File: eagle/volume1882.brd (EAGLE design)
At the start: 48.3 x 48.3 mm, 39 parts, among them IC1 LM317, IC2 LM337, U1 DS1882, U2 ATMEGA328P_TQFP

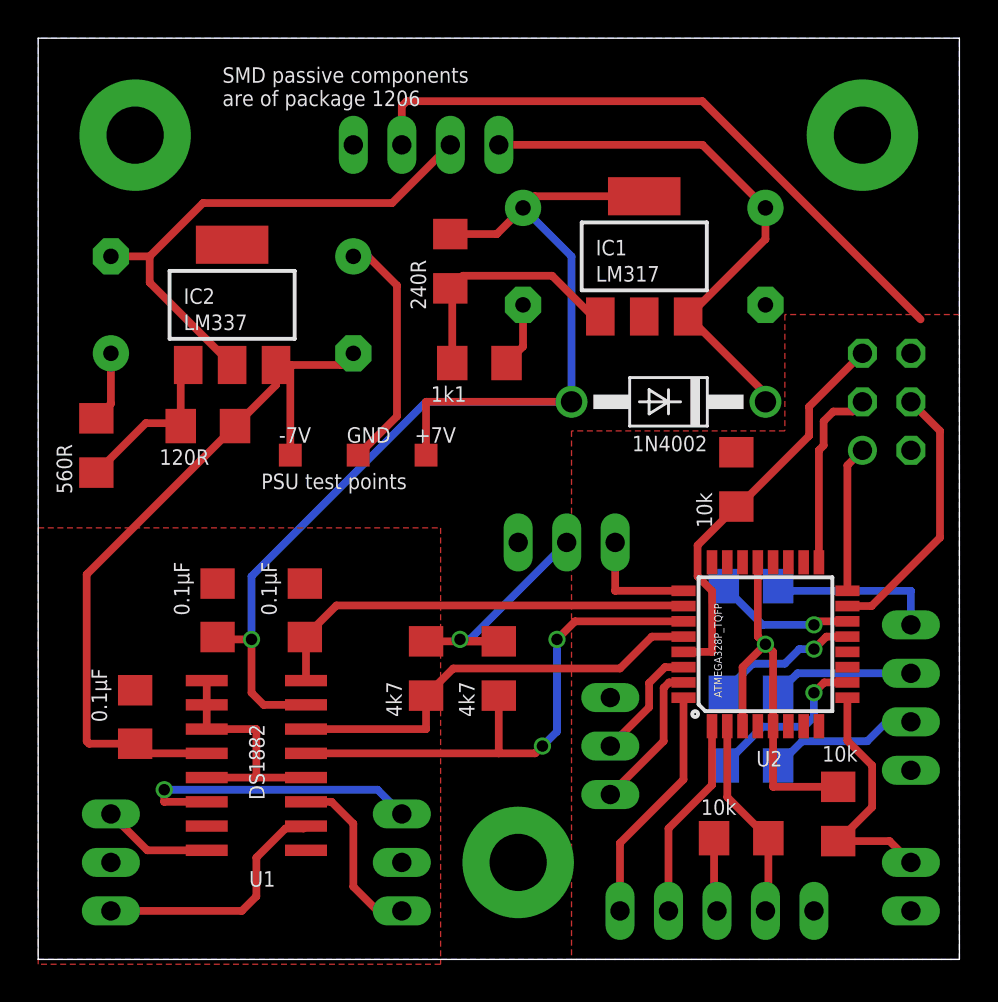
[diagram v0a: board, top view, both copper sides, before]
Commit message: fixed wrong size parts
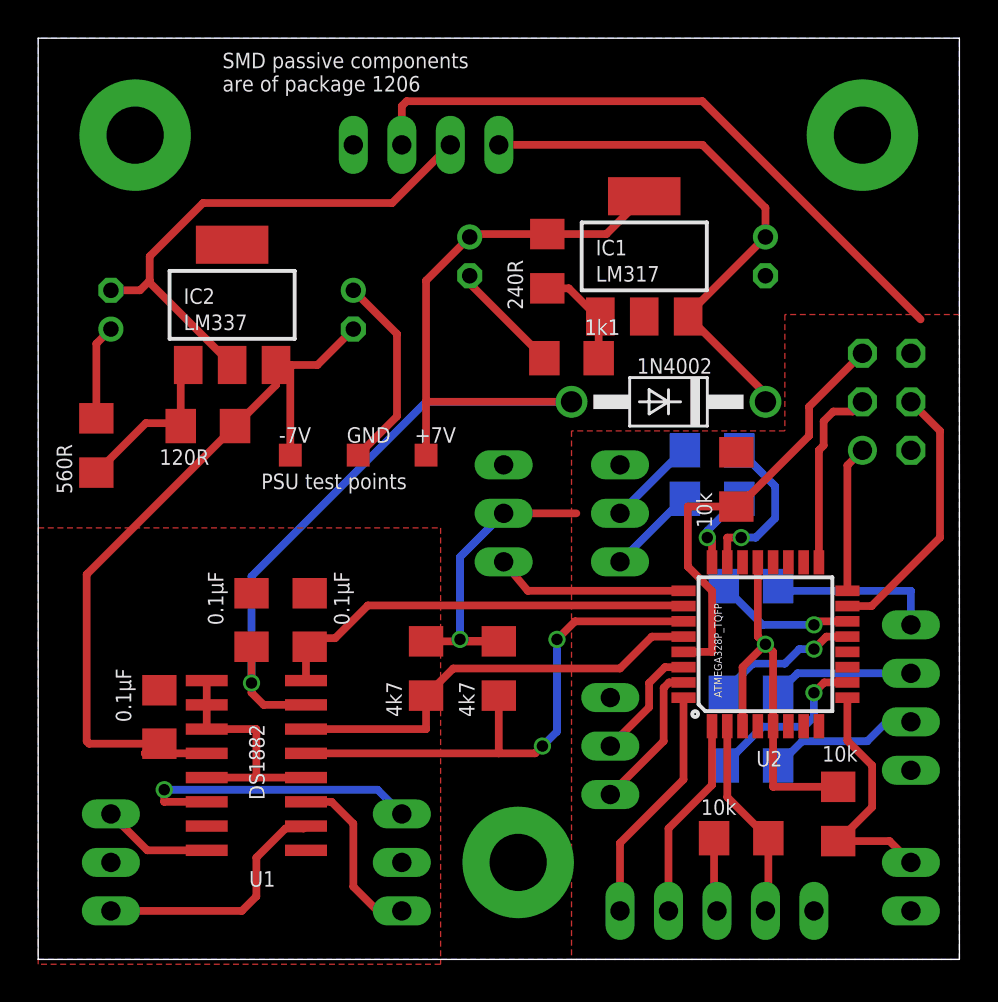
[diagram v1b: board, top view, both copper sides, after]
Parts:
- removed C4: 0.1µF, resistor:E5-5
- removed C5, C6: 1µF, resistor:E5-5
- removed C7: 10µF, resistor:E5-5
- added C10, C8: 1µF, resistor:E2-5
- added C11: 0.1µF, resistor:E2-5
- added C9: 10µF, resistor:E2-5
- added LED_OUTPUT: (no value), con-lstb:MA03-1
- added R13, R14: 470R, resistor:R1206
- moved R4 5.08 mm to (26.7, 36.6)
- moved R6 4.83 mm to (27.9, 31.5), turned to 180 degrees
- moved RELAY 3.64 mm to (24.4, 23.4), turned to 90 degrees
- moved C2 1.85 mm to (11.2, 17.8)
- moved C3 1.27 mm to (6.35, 12.7)
- moved C1 0.57 mm to (14.2, 17.8)
- renumbered LED to LED_VOLUME
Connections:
- new net N$29: R13.1, U2.23
- new net N$30: R14.1, U2.24
- new net N$31: LED_OUTPUT.2, R13.2
- new net N$32: LED_OUTPUT.3, R14.2
- net GND: now also C10.-, C11.-, C8.+, C9.+, LED_OUTPUT.1; no longer C4.-, C5.-, C6.+, C7.+
- net N$20: now also C11.+; no longer C4.+
- net N$21: now also C8.-; no longer C6.-
- net V+: now also C10.+; no longer C5.+
- net V-: now also C9.-; no longer C7.-
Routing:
- net N$29: track 0.00 -> 8.56 mm, vias 0 -> 1
- net N$22: track 13.0 -> 5.56 mm
- net N$31: track 0.00 -> 4.77 mm
- net N$32: track 0.00 -> 4.77 mm
- net N$30: track 0.00 -> 4.26 mm, vias 0 -> 1
- net N$25: track 6.12 -> 10.1 mm
- net VCC: track 47.6 -> 51.3 mm
- net V+: track 64.2 -> 61.9 mm
- net V-: track 39.4 -> 41.4 mm
- net N$1: track 21.1 -> 23.0 mm
- net GND: track 56.8 -> 58.3 mm
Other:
- board text added: "1"
- board text added: "2"
- board text added: "TRIG"
- board text removed: "IO"

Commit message: small fixes
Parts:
- added REMOTE: (no value), con-lstb:MA03-1
- moved ICSP 3.30 mm to (44.5, 25.9)
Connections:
- new net N$33: REMOTE.1, U2.12
- net GND: now also REMOTE.2
- net VCC: now also REMOTE.3
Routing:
- net N$33: track 0.00 -> 32.8 mm, vias 0 -> 1
- net N$4: track 14.1 -> 9.67 mm
- net N$3: track 9.95 -> 6.05 mm
- net N$2: track 7.69 -> 4.38 mm
- net GND: track 58.3 -> 55.8 mm
- net N$1: track 23.0 -> 20.7 mm
- net VCC: track 51.3 -> 49.3 mm
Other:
- board text added: "Digital volume control and pre-amp controls Version 0.1 Revision 1 Audio signal must not exceed +/- 7V Designed June 2016 by Iver Egge"
- board text removed: "Digital volume control v0.1 Revision 1 Audio signal must not exceed +/- 7V Designed June 2016 by Iver Egge"
